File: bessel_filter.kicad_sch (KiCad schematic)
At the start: 7 parts, among them J1 Conn_Coaxial, J2 Conn_Coaxial

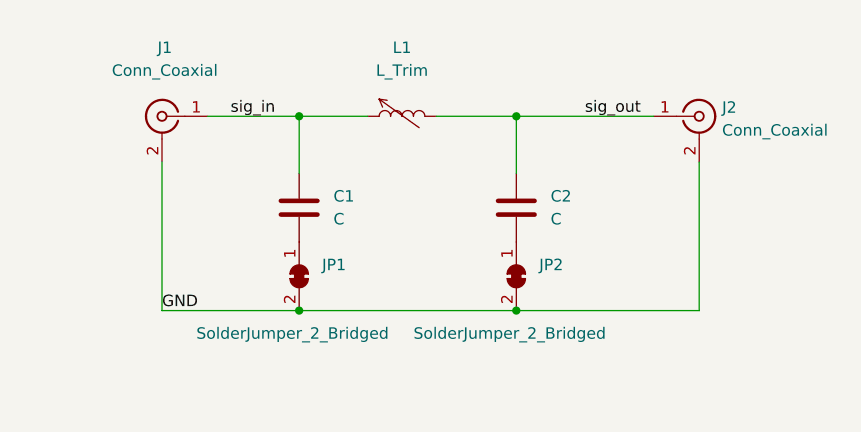
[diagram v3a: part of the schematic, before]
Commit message: progress on PCB--need to add L shield to ground connections
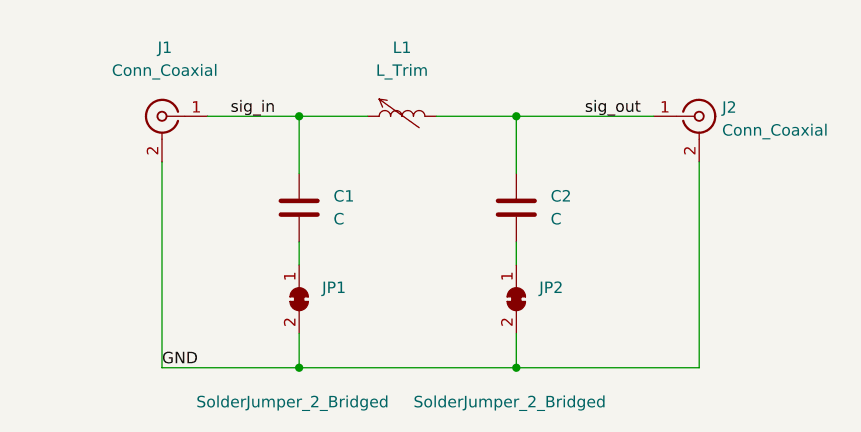
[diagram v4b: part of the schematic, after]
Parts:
- C1, C2: footprint (none) -> Capacitor_SMD:C_1206_3216Metric_Pad1.33x1.80mm_HandSolder
- J1, J2: footprint (none) -> Connector_Coaxial:SMA_Amphenol_132289_EdgeMount
- JP1: footprint TestPoint:TestPoint_Bridge_Pitch2.0mm_Drill0.7mm -> Jumper:SolderJumper-2_P1.3mm_Open_TrianglePad1.0x1.5mm
- JP2: footprint (none) -> Jumper:SolderJumper-2_P1.3mm_Open_TrianglePad1.0x1.5mm
- L1: footprint (none) -> HugonLib:Coil_Craft_Unicoil_10mm
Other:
- moved on the sheet: JP1, JP2
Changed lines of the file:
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@@
   (junction (at 153.67 92.71) (diameter 0) (color 0 0 0 0)
   )
-  (junction (at 129.54 114.3) (diameter 0) (color 0 0 0 0)
+  (junction (at 129.54 120.65) (diameter 0) (color 0 0 0 0)
   )
   (junction (at 129.54 92.71) (diameter 0) (color 0 0 0 0)
   )
-  (junction (at 153.67 114.3) (diameter 0) (color 0 0 0 0)
+  (junction (at 153.67 120.65) (diameter 0) (color 0 0 0 0)
   )
   (wire (pts (xy 119.38 92.71) (xy 129.54 92.71))
     (stroke (width 0) (type default) (color 0 0 0 0))
   )
-  (wire (pts (xy 114.3 114.3) (xy 129.54 114.3))
-    (stroke (width 0) (type default) (color 0 0 0 0))
-  )
-  (wire (pts (xy 129.54 114.3) (xy 153.67 114.3))
-    (stroke (width 0) (type default) (color 0 0 0 0))
-  )
-  (wire (pts (xy 173.99 114.3) (xy 173.99 97.79))
+  (wire (pts (xy 114.3 120.65) (xy 129.54 120.65))
+    (stroke (width 0) (type default) (color 0 0 0 0))
+  )
+  (wire (pts (xy 129.54 120.65) (xy 153.67 120.65))
+    (stroke (width 0) (type default) (color 0 0 0 0))
+  )
+  (wire (pts (xy 129.54 109.22) (xy 129.54 106.68))
+    (stroke (width 0) (type default) (color 0 0 0 0))
+  )
+  (wire (pts (xy 129.54 116.84) (xy 129.54 120.65))
+    (stroke (width 0) (type default) (color 0 0 0 0))
+  )
+  (wire (pts (xy 153.67 116.84) (xy 153.67 120.65))
+    (stroke (width 0) (type default) (color 0 0 0 0))
+  )
+  (wire (pts (xy 173.99 120.65) (xy 173.99 97.79))
     (stroke (width 0) (type default) (color 0 0 0 0))
   )
@@
     (stroke (width 0) (type default) (color 0 0 0 0))
   )
-  (wire (pts (xy 153.67 114.3) (xy 173.99 114.3))
-    (stroke (width 0) (type default) (color 0 0 0 0))
-  )
-  (wire (pts (xy 114.3 97.79) (xy 114.3 114.3))
+  (wire (pts (xy 153.67 109.22) (xy 153.67 106.68))
+    (stroke (width 0) (type default) (color 0 0 0 0))
+  )
+  (wire (pts (xy 153.67 120.65) (xy 173.99 120.65))
+    (stroke (width 0) (type default) (color 0 0 0 0))
+  )
+  (wire (pts (xy 114.3 97.79) (xy 114.3 120.65))
     (stroke (width 0) (type default) (color 0 0 0 0))
   )
@@
     (effects (font (size 1.27 1.27)) (justify left bottom))
   )
-  (label "GND" (at 114.3 114.3 0)
+  (label "GND" (at 114.3 120.65 0)
     (effects (font (size 1.27 1.27)) (justify left bottom))
   )
@@
       (effects (font (size 1.27 1.27)) (justify left))
     )
-    (property "Footprint" "" (id 2) (at 154.6352 106.68 0)
+    (property "Footprint" "Capacitor_SMD:C_1206_3216Metric_Pad1.33x1.80mm_HandSolder" (id 2) (at 154.6352 106.68 0)
       (effects (font (size 1.27 1.27)) hide)
     )
@@
     (pin "2")
   )
-  (symbol (lib_id "Jumper:SolderJumper_2_Bridged") (at 153.67 110.49 270) (unit 1)
+  (symbol (lib_id "Jumper:SolderJumper_2_Bridged") (at 153.67 113.03 270) (unit 1)
     (in_bom yes) (on_board yes)
-    (property "Reference" "JP2" (id 0) (at 156.21 109.2199 90)
-      (effects (font (size 1.27 1.27)) (justify left))
-    )
-    (property "Value" "SolderJumper_2_Bridged" (id 1) (at 142.24 116.84 90)
-      (effects (font (size 1.27 1.27)) (justify left))
-    )
-    (property "Footprint" "" (id 2) (at 153.67 110.49 0)
-      (effects (font (size 1.27 1.27)) hide)
-    )
-    (property "Datasheet" "~" (id 3) (at 153.67 110.49 0)
+    (property "Reference" "JP2" (id 0) (at 156.21 111.7599 90)
+      (effects (font (size 1.27 1.27)) (justify left))
+    )
+    (property "Value" "SolderJumper_2_Bridged" (id 1) (at 142.24 124.46 90)
+      (effects (font (size 1.27 1.27)) (justify left))
+    )
+    (property "Footprint" "Jumper:SolderJumper-2_P1.3mm_Open_TrianglePad1.0x1.5mm" (id 2) (at 153.67 113.03 0)
+      (effects (font (size 1.27 1.27)) hide)
+    )
+    (property "Datasheet" "~" (id 3) (at 153.67 113.03 0)
       (effects (font (size 1.27 1.27)) hide)
     )
@@
     (property "Reference" "L1" (id 0) (at 140.97 85.09 90))
     (property "Value" "L_Trim" (id 1) (at 140.97 87.63 90))
-    (property "Footprint" "" (id 2) (at 140.97 92.71 0)
+    (property "Footprint" "HugonLib:Coil_Craft_Unicoil_10mm" (id 2) (at 140.97 92.71 0)
       (effects (font (size 1.27 1.27)) hide)
     )
@@
     (property "Reference" "J1" (id 0) (at 114.6174 85.09 0))
     (property "Value" "Conn_Coaxial" (id 1) (at 114.6174 87.63 0))
-    (property "Footprint" "" (id 2) (at 114.3 92.71 0)
+    (property "Footprint" "Connector_Coaxial:SMA_Amphenol_132289_EdgeMount" (id 2) (at 114.3 92.71 0)
       (effects (font (size 1.27 1.27)) hide)
     )
@@
     (pin "2")
   )
-  (symbol (lib_id "Jumper:SolderJumper_2_Bridged") (at 129.54 110.49 270) (unit 1)
+  (symbol (lib_id "Jumper:SolderJumper_2_Bridged") (at 129.54 113.03 270) (unit 1)
     (in_bom yes) (on_board yes)
-    (property "Reference" "JP1" (id 0) (at 132.08 109.2199 90)
-      (effects (font (size 1.27 1.27)) (justify left))
-    )
-    (property "Value" "SolderJumper_2_Bridged" (id 1) (at 118.11 116.84 90)
-      (effects (font (size 1.27 1.27)) (justify left))
-    )
-    (property "Footprint" "TestPoint:TestPoint_Bridge_Pitch2.0mm_Drill0.7mm" (id 2) (at 129.54 110.49 0)
-      (effects (font (size 1.27 1.27)) hide)
-    )
-    (property "Datasheet" "~" (id 3) (at 129.54 110.49 0)
+    (property "Reference" "JP1" (id 0) (at 132.08 111.7599 90)
+      (effects (font (size 1.27 1.27)) (justify left))
+    )
+    (property "Value" "SolderJumper_2_Bridged" (id 1) (at 118.11 124.46 90)
+      (effects (font (size 1.27 1.27)) (justify left))
+    )
+    (property "Footprint" "Jumper:SolderJumper-2_P1.3mm_Open_TrianglePad1.0x1.5mm" (id 2) (at 129.54 113.03 0)
+      (effects (font (size 1.27 1.27)) hide)
+    )
+    (property "Datasheet" "~" (id 3) (at 129.54 113.03 0)
       (effects (font (size 1.27 1.27)) hide)
     )
@@
       (effects (font (size 1.27 1.27)) (justify left))
     )
-    (property "Footprint" "" (id 2) (at 130.5052 106.68 0)
+    (property "Footprint" "Capacitor_SMD:C_1206_3216Metric_Pad1.33x1.80mm_HandSolder" (id 2) (at 130.5052 106.68 0)
       (effects (font (size 1.27 1.27)) hide)
     )
@@
       (effects (font (size 1.27 1.27)) (justify left))
     )
-    (property "Footprint" "" (id 2) (at 173.99 92.71 0)
+    (property "Footprint" "Connector_Coaxial:SMA_Amphenol_132289_EdgeMount" (id 2) (at 173.99 92.71 0)
       (effects (font (size 1.27 1.27)) hide)
     )
@@
   (symbol_instances
     (path "/c02ac052-0eb1-4e20-ad3f-f8b1c6ef6429"
-      (reference "C1") (unit 1) (value "C") (footprint "")
+      (reference "C1") (unit 1) (value "C") (footprint "Capacitor_SMD:C_1206_3216Metric_Pad1.33x1.80mm_HandSolder")
     )
     (path "/3954301a-53c0-4509-a36a-1f3f611bbf6a"
-      (reference "C2") (unit 1) (value "C") (footprint "")
+      (reference "C2") (unit 1) (value "C") (footprint "Capacitor_SMD:C_1206_3216Metric_Pad1.33x1.80mm_HandSolder")
     )
     (path "/90d228ac-5ec9-4302-b393-9e4058ef8745"
-      (reference "J1") (unit 1) (value "Conn_Coaxial") (footprint "")
+      (reference "J1") (unit 1) (value "Conn_Coaxial") (footprint "Connector_Coaxial:SMA_Amphenol_132289_EdgeMount")
     )
     (path "/f23ff5c1-67ee-41ec-99a6-6a21a3430465"
-      (reference "J2") (unit 1) (value "Conn_Coaxial") (footprint "")
+      (reference "J2") (unit 1) (value "Conn_Coaxial") (footprint "Connector_Coaxial:SMA_Amphenol_132289_EdgeMount")
     )
     (path "/96921448-aacb-48d2-98d0-e1759ed54dc6"
-      (reference "JP1") (unit 1) (value "SolderJumper_2_Bridged") (footprint "TestPoint:TestPoint_Bridge_Pitch2.0mm_Drill0.7mm")
+      (reference "JP1") (unit 1) (value "SolderJumper_2_Bridged") (footprint "Jumper:SolderJumper-2_P1.3mm_Open_TrianglePad1.0x1.5mm")
     )
     (path "/860f9371-2878-4c51-abb3-438c3412d534"
-      (reference "JP2") (unit 1) (value "SolderJumper_2_Bridged") (footprint "")
+      (reference "JP2") (unit 1) (value "SolderJumper_2_Bridged") (footprint "Jumper:SolderJumper-2_P1.3mm_Open_TrianglePad1.0x1.5mm")
     )
     (path "/867a4a3d-7555-41bb-964a-c09677a9fea2"
-      (reference "L1") (unit 1) (value "L_Trim") (footprint "")
-    )
-  )
+      (reference "L1") (unit 1) (value "L_Trim") (footprint "HugonLib:Coil_Craft_Unicoil_10mm")
+    )
+  )

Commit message: Finished layout for 3rd order-fixed L
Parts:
- removed JP1, JP2: SolderJumper_2_Bridged, Jumper:SolderJumper-2_P1.3mm_Open_TrianglePad1.0x1.5mm, symbol Jumper:SolderJumper_2_Bridged
- L1: value L_Trim -> L; footprint HugonLib:Coil_Craft_Unicoil_10mm -> Inductor_SMD:L_1206_3216Metric_Pad1.42x1.75mm_HandSolder; symbol Device:L_Trim -> Device:L
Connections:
- net GND: now also C1.2, C2.2
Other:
- note removed: "3rd order Bessel Pi-network low-pass filter i/o impedance is 50 ohm See README.md for component values"
- title: Bessel Filter -> LC Filter 3rd Order
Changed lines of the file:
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@@
   (paper "USLetter")
   (title_block
-    (title "Bessel Filter")
-    (date "2022-03-13")
+    (title "LC Filter 3rd Order")
+    (date "2022-03-14")
     (rev "1.0")
     (company "HugonLabs")
@@
     (stroke (width 0) (type default) (color 0 0 0 0))
   )
-  (wire (pts (xy 129.54 109.22) (xy 129.54 106.68))
-    (stroke (width 0) (type default) (color 0 0 0 0))
-  )
-  (wire (pts (xy 129.54 116.84) (xy 129.54 120.65))
-    (stroke (width 0) (type default) (color 0 0 0 0))
-  )
-  (wire (pts (xy 153.67 116.84) (xy 153.67 120.65))
+  (wire (pts (xy 129.54 106.68) (xy 129.54 120.65))
     (stroke (width 0) (type default) (color 0 0 0 0))
   )
@@
     (stroke (width 0) (type default) (color 0 0 0 0))
   )
-  (wire (pts (xy 153.67 109.22) (xy 153.67 106.68))
+  (wire (pts (xy 153.67 106.68) (xy 153.67 120.65))
     (stroke (width 0) (type default) (color 0 0 0 0))
   )
@@
   (wire (pts (xy 129.54 92.71) (xy 137.16 92.71))
     (stroke (width 0) (type default) (color 0 0 0 0))
-  )
-  (text "3rd order Bessel Pi-network low-pass filter\ni/o impedance is 50 ohm\nSee README.md for component values"
-    (at 12.7 19.05 0)
-    (effects (font (size 1.27 1.27)) (justify left bottom))
   )
   (label "sig_in" (at 121.92 92.71 0)
@@
     (pin "2")
   )
-  (symbol (lib_id "Jumper:SolderJumper_2_Bridged") (at 153.67 113.03 270) (unit 1)
-    (in_bom yes) (on_board yes)
-    (property "Reference" "JP2" (id 0) (at 156.21 111.7599 90)
-      (effects (font (size 1.27 1.27)) (justify left))
-    )
-    (property "Value" "SolderJumper_2_Bridged" (id 1) (at 142.24 124.46 90)
-      (effects (font (size 1.27 1.27)) (justify left))
-    )
-    (property "Footprint" "Jumper:SolderJumper-2_P1.3mm_Open_TrianglePad1.0x1.5mm" (id 2) (at 153.67 113.03 0)
-      (effects (font (size 1.27 1.27)) hide)
-    )
-    (property "Datasheet" "~" (id 3) (at 153.67 113.03 0)
-      (effects (font (size 1.27 1.27)) hide)
-    )
-    (pin "1")
-    (pin "2")
-  )
-  (symbol (lib_id "Device:L_Trim") (at 140.97 92.71 90) (unit 1)
+  (symbol (lib_id "Device:L") (at 140.97 92.71 90) (unit 1)
     (in_bom yes) (on_board yes) (fields_autoplaced)
-    (property "Reference" "L1" (id 0) (at 140.97 85.09 90))
-    (property "Value" "L_Trim" (id 1) (at 140.97 87.63 90))
-    (property "Footprint" "HugonLib:Coil_Craft_Unicoil_10mm" (id 2) (at 140.97 92.71 0)
+    (property "Reference" "L1" (id 0) (at 140.97 86.36 90))
+    (property "Value" "L" (id 1) (at 140.97 88.9 90))
+    (property "Footprint" "Inductor_SMD:L_1206_3216Metric_Pad1.42x1.75mm_HandSolder" (id 2) (at 140.97 92.71 0)
       (effects (font (size 1.27 1.27)) hide)
     )
@@
     )
     (property "Datasheet" " ~" (id 3) (at 114.3 92.71 0)
-      (effects (font (size 1.27 1.27)) hide)
-    )
-    (pin "1")
-    (pin "2")
-  )
-  (symbol (lib_id "Jumper:SolderJumper_2_Bridged") (at 129.54 113.03 270) (unit 1)
-    (in_bom yes) (on_board yes)
-    (property "Reference" "JP1" (id 0) (at 132.08 111.7599 90)
-      (effects (font (size 1.27 1.27)) (justify left))
-    )
-    (property "Value" "SolderJumper_2_Bridged" (id 1) (at 118.11 124.46 90)
-      (effects (font (size 1.27 1.27)) (justify left))
-    )
-    (property "Footprint" "Jumper:SolderJumper-2_P1.3mm_Open_TrianglePad1.0x1.5mm" (id 2) (at 129.54 113.03 0)
-      (effects (font (size 1.27 1.27)) hide)
-    )
-    (property "Datasheet" "~" (id 3) (at 129.54 113.03 0)
       (effects (font (size 1.27 1.27)) hide)
     )
@@
       (reference "J2") (unit 1) (value "Conn_Coaxial") (footprint "Connector_Coaxial:SMA_Amphenol_132289_EdgeMount")
     )
-    (path "/96921448-aacb-48d2-98d0-e1759ed54dc6"
-      (reference "JP1") (unit 1) (value "SolderJumper_2_Bridged") (footprint "Jumper:SolderJumper-2_P1.3mm_Open_TrianglePad1.0x1.5mm")
-    )
-    (path "/860f9371-2878-4c51-abb3-438c3412d534"
-      (reference "JP2") (unit 1) (value "SolderJumper_2_Bridged") (footprint "Jumper:SolderJumper-2_P1.3mm_Open_TrianglePad1.0x1.5mm")
-    )
     (path "/867a4a3d-7555-41bb-964a-c09677a9fea2"
-      (reference "L1") (unit 1) (value "L_Trim") (footprint "HugonLib:Coil_Craft_Unicoil_10mm")
+      (reference "L1") (unit 1) (value "L") (footprint "Inductor_SMD:L_1206_3216Metric_Pad1.42x1.75mm_HandSolder")
     )
   )
